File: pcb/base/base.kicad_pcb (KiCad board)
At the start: 2 copper layers, 80 x 100 mm, 38 parts, among them J1 Conn_01x03_Pin, J2 Screw_Terminal_01x04, J3 Screw_Terminal_01x02, K1 Relay_SPDT, K2 Relay_SPDT, K3 Relay_SPDT, K4 Relay_SPDT, Q1 NMOS, Q2 NMOS, Q3 NMOS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

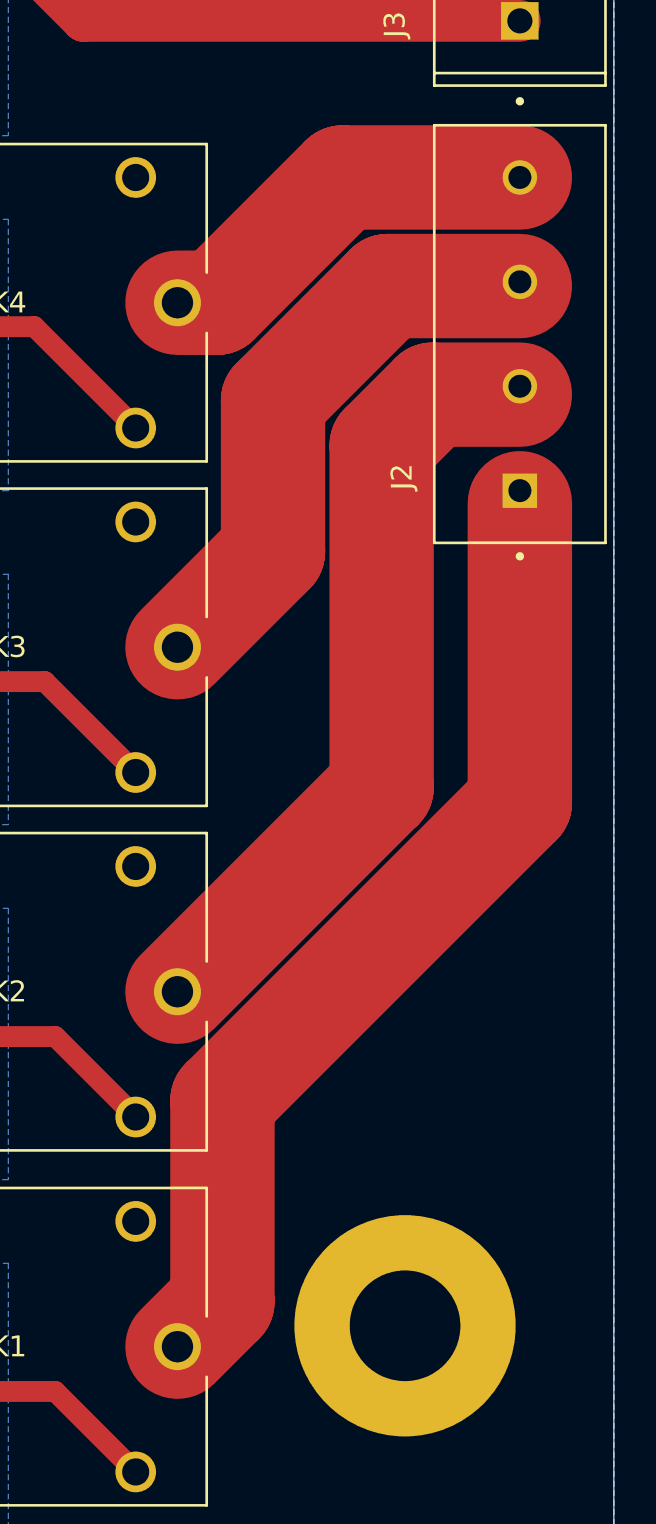
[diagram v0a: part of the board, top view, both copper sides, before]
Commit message: Update some trace widths
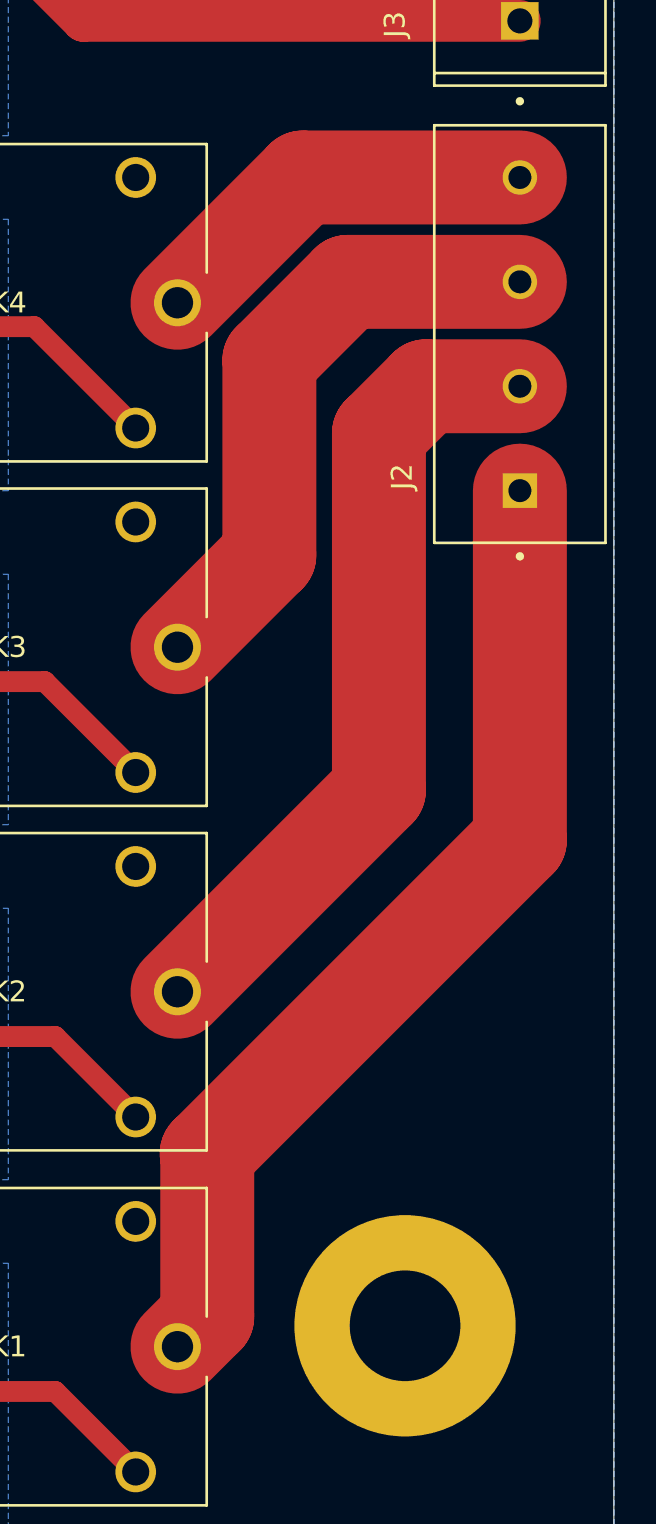
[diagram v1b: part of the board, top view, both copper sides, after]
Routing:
- net /Rail3: track 27.8 -> 29.1 mm
- net /Rail1: track 47.2 -> 47.8 mm
- net /Rail2: track 37.8 -> 38.4 mm
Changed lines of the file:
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@@
 	)
 	(segment
-		(start 129.1 121)
-		(end 131 121)
-		(width 5)
+		(start 135.1 115)
+		(end 145.5 115)
+		(width 4.5)
 		(layer "F.Cu")
 		(net 12)
 	)
 	(segment
-		(start 137 115)
-		(end 145.5 115)
-		(width 5)
+		(start 129.1 121)
+		(end 135.1 115)
+		(width 4.5)
 		(layer "F.Cu")
 		(net 12)
 	)
 	(segment
-		(start 131 121)
-		(end 137 115)
-		(width 5)
-		(layer "F.Cu")
-		(net 12)
-	)
-	(segment
-		(start 138.878663 144.221337)
-		(end 138.878663 127.831986)
-		(width 5)
+		(start 138.75 127.25)
+		(end 141 125)
+		(width 4.5)
 		(layer "F.Cu")
 		(net 13)
 	)
 	(segment
-		(start 138.878663 127.831986)
-		(end 141.308649 125.402)
-		(width 5)
+		(start 141 125)
+		(end 145.5 125)
+		(width 4.5)
 		(layer "F.Cu")
 		(net 13)
@@
 	(segment
 		(start 129.1 154)
-		(end 138.878663 144.221337)
-		(width 5)
+		(end 138.75 144.35)
+		(width 4.5)
 		(layer "F.Cu")
 		(net 13)
 	)
 	(segment
-		(start 141.308649 125.402)
-		(end 145.5 125.402)
-		(width 5)
+		(start 138.75 144.35)
+		(end 138.75 127.25)
+		(width 4.5)
 		(layer "F.Cu")
 		(net 13)
 	)
 	(segment
-		(start 133.677663 125.677662)
-		(end 139.154325 120.201)
-		(width 5)
+		(start 133.5 123.75)
+		(end 137.25 120)
+		(width 4.5)
+		(layer "F.Cu")
+		(net 14)
+	)
+	(segment
+		(start 133.5 133.1)
+		(end 133.5 123.75)
+		(width 4.5)
+		(layer "F.Cu")
+		(net 14)
+	)
+	(segment
+		(start 137.25 120)
+		(end 145.5 120)
+		(width 4.5)
 		(layer "F.Cu")
 		(net 14)
@@
 	(segment
 		(start 129.1 137.5)
-		(end 133.677663 132.922337)
-		(width 5)
+		(end 133.5 133.1)
+		(width 4.5)
 		(layer "F.Cu")
 		(net 14)
 	)
 	(segment
-		(start 139.154325 120.201)
-		(end 145.5 120.201)
-		(width 5)
-		(layer "F.Cu")
-		(net 14)
-	)
-	(segment
-		(start 133.677663 132.922337)
-		(end 133.677663 125.677662)
-		(width 5)
-		(layer "F.Cu")
-		(net 14)
-	)
-	(segment
-		(start 129.1 171)
-		(end 131.254324 168.845676)
-		(width 5)
+		(start 145.5 130)
+		(end 145.5 146.75)
+		(width 4.5)
 		(layer "F.Cu")
 		(net 15)
 	)
 	(segment
-		(start 131.254324 168.845676)
-		(end 131.254324 159.201)
-		(width 5)
+		(start 130.526 161.776)
+		(end 130.526 169.574)
+		(width 4.5)
 		(layer "F.Cu")
 		(net 15)
 	)
 	(segment
-		(start 145.5 144.955324)
-		(end 145.5 130.603)
-		(width 5)
+		(start 130.5 161.75)
+		(end 130.526 161.776)
+		(width 4.5)
 		(layer "F.Cu")
 		(net 15)
 	)
 	(segment
-		(start 131.254324 159.201)
-		(end 145.5 144.955324)
-		(width 5)
+		(start 145.5 146.75)
+		(end 130.5 161.75)
+		(width 4.5)
 		(layer "F.Cu")
 		(net 15)
+	)
+	(segment
+		(start 130.526 169.574)
+		(end 129.1 171)
+		(width 4.5)
+		(layer "F.Cu")
+		(net 15)
